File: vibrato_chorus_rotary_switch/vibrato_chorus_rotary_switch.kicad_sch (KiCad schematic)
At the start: 2 parts, among them J1 7-215079-8, SW1 SW_Rotary1x6

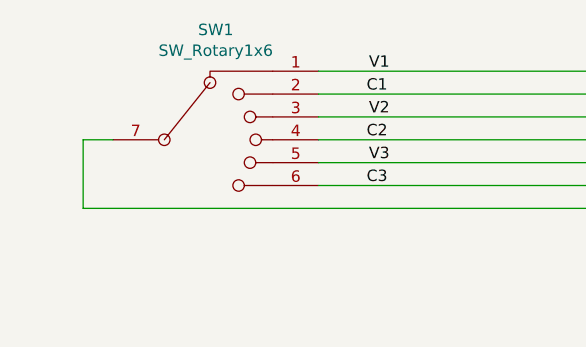
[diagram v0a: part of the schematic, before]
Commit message: A very small PCB to handle the V/C rotary switch selector
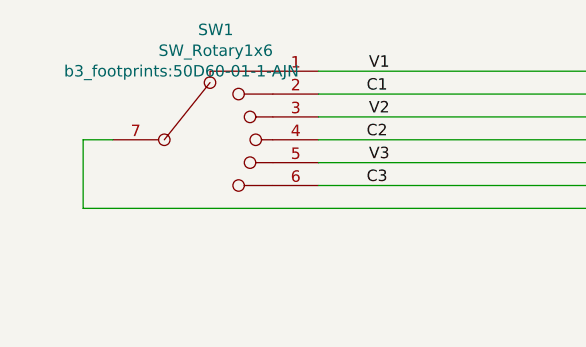
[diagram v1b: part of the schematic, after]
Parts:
- J1: footprint b3_footprints:MicroMatch_2x04_P1.27mm_Vertical -> Connector_TE-Connectivity:TE_Micro-MaTch_215079-8_2x04_P1.27mm_Vertical

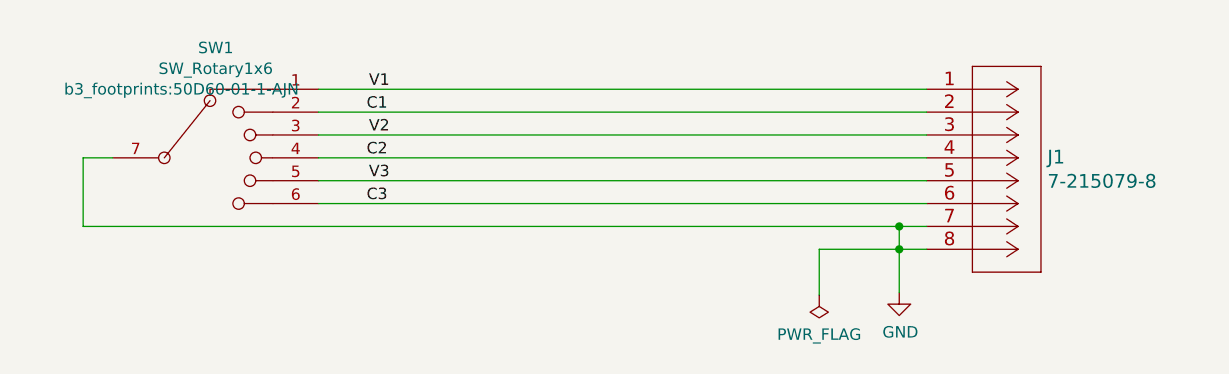
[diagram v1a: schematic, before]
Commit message: The V/C rotary switch is now connected to the new mother board.
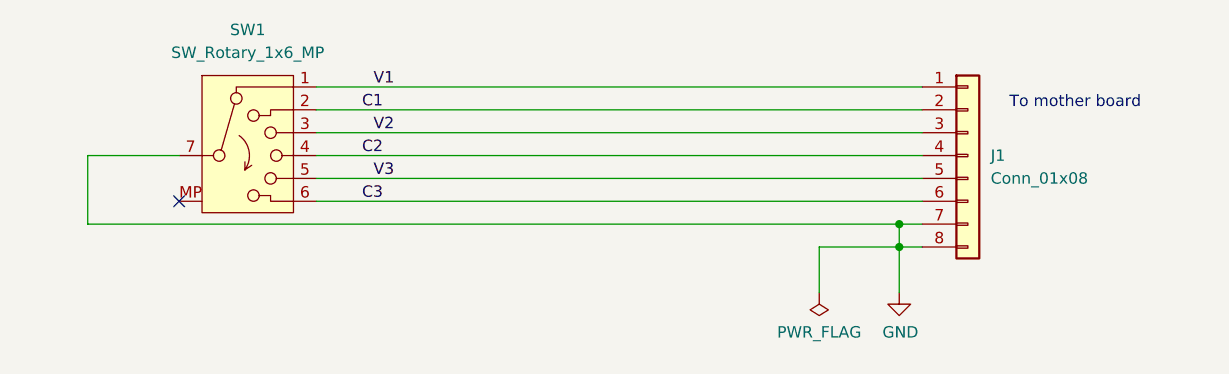
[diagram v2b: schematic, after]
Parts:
- removed J1: 7-215079-8, Connector_TE-Connectivity:TE_Micro-MaTch_215079-8_2x04_P1.27mm_Vertical, symbol b3_connectors_library:7-215079-8
- removed SW1: SW_Rotary1x6, b3_footprints:50D60-01-1-AJN, symbol schematic_library:SW_Rotary1x6
- added J1: Conn_01x08, symbol Connector_Generic:Conn_01x08
- added SW1: SW_Rotary_1x6_MP, symbol Switch:SW_Rotary_1x6_MP
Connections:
- net C1: now also J1.2 (Pin_2), SW1.2
- net C2: now also J1.4 (Pin_4), SW1.4
- net C3: now also J1.6 (Pin_6), SW1.6
- net GND: now also J1.7 (Pin_7), J1.8 (Pin_8), SW1.7
- net V1: now also J1.1 (Pin_1), SW1.1
- net V2: now also J1.3 (Pin_3), SW1.3
- net V3: now also J1.5 (Pin_5), SW1.5
- no-connect marks 0 -> 1
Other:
- note added: "To mother board"

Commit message: New organ architecture with mother board
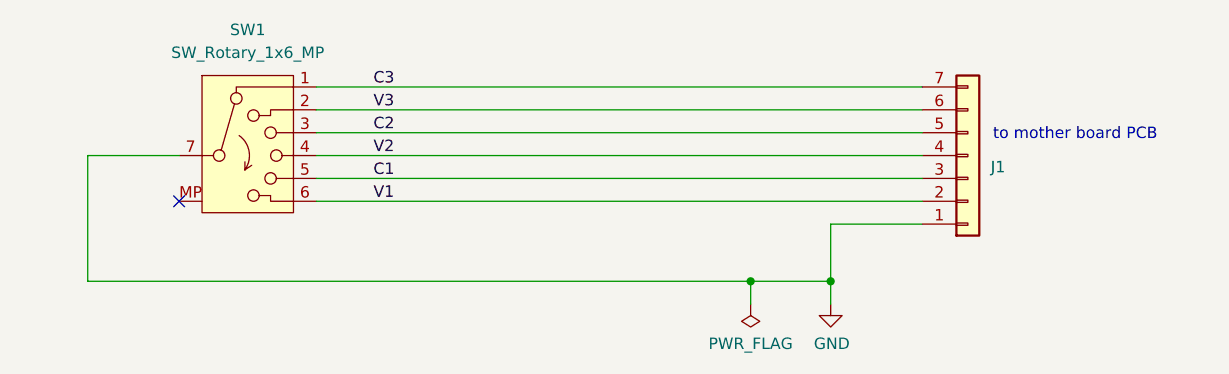
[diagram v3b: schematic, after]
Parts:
- removed J1: Conn_01x08, symbol Connector_Generic:Conn_01x08
- added J1: Conn_01x07, symbol Connector_Generic:Conn_01x07
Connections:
- net C1: now also SW1.5, J1.3 (Pin_3); no longer SW1.2
- net C2: now also SW1.3, J1.5 (Pin_5); no longer SW1.4
- net C3: now also SW1.1, J1.7 (Pin_7); no longer SW1.6
- net GND: now also J1.1 (Pin_1)
- net V1: now also SW1.6, J1.2 (Pin_2); no longer SW1.1
- net V2: now also SW1.4, J1.4 (Pin_4); no longer SW1.3
- net V3: now also SW1.2, J1.6 (Pin_6); no longer SW1.5
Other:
- note added: "to mother board PCB"
- note removed: "To mother board"
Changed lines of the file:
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@@
 (kicad_sch
-	(version 20231120)
+	(version 20250114)
 	(generator "eeschema")
-	(generator_version "8.0")
+	(generator_version "9.0")
 	(paper "A4")
 	(title_block
@@
 		(date "2024-11-12")
 	)
+	(text "to mother board PCB"
+		(exclude_from_sim no)
+		(at 203.454 90.424 0)
+		(effects
+			(font
+				(size 1.27 1.27)
+			)
+			(justify left)
+		)
+	)
 	(junction
-		(at 193.04 100.33)
+		(at 185.42 106.68)
 		(diameter 0)
 		(color 0 0 0 0)
 	)
 	(junction
-		(at 193.04 102.87)
+		(at 176.53 106.68)
 		(diameter 0)
 		(color 0 0 0 0)
@@
 	(wire
 		(pts
-			(xy 102.87 100.33) (xy 193.04 100.33)
-		)
-		(stroke
-			(width 0)
-			(type default)
-		)
-	)
-	(wire
-		(pts
-			(xy 102.87 92.71) (xy 102.87 100.33)
+			(xy 102.87 106.68) (xy 176.53 106.68)
+		)
+		(stroke
+			(width 0)
+			(type default)
+		)
+	)
+	(wire
+		(pts
+			(xy 102.87 92.71) (xy 102.87 106.68)
+		)
+		(stroke
+			(width 0)
+			(type default)
+		)
+	)
+	(wire
+		(pts
+			(xy 185.42 100.33) (xy 195.58 100.33)
 		)
 		(stroke
@@
 	(wire
 		(pts
+			(xy 185.42 106.68) (xy 185.42 109.22)
+		)
+		(stroke
+			(width 0)
+			(type default)
+		)
+	)
+	(wire
+		(pts
 			(xy 128.27 87.63) (xy 195.58 87.63)
 		)
@@
 	(wire
 		(pts
-			(xy 193.04 100.33) (xy 195.58 100.33)
-		)
-		(stroke
-			(width 0)
-			(type default)
-		)
-	)
-	(wire
-		(pts
-			(xy 193.04 102.87) (xy 193.04 107.95)
+			(xy 128.27 95.25) (xy 195.58 95.25)
+		)
+		(stroke
+			(width 0)
+			(type default)
+		)
+	)
+	(wire
+		(pts
+			(xy 185.42 100.33) (xy 185.42 106.68)
 		)
 		(stroke
@@
 	(wire
 		(pts
-			(xy 184.15 107.95) (xy 184.15 102.87)
-		)
-		(stroke
-			(width 0)
-			(type default)
-		)
-	)
-	(wire
-		(pts
-			(xy 184.15 102.87) (xy 193.04 102.87)
-		)
-		(stroke
-			(width 0)
-			(type default)
-		)
-	)
-	(wire
-		(pts
-			(xy 195.58 95.25) (xy 128.27 95.25)
-		)
-		(stroke
-			(width 0)
-			(type default)
-		)
-	)
-	(wire
-		(pts
-			(xy 195.58 102.87) (xy 193.04 102.87)
-		)
-		(stroke
-			(width 0)
-			(type default)
-		)
-	)
-	(wire
-		(pts
-			(xy 195.58 90.17) (xy 128.27 90.17)
-		)
-		(stroke
-			(width 0)
-			(type default)
-		)
-	)
-	(wire
-		(pts
-			(xy 193.04 102.87) (xy 193.04 100.33)
-		)
-		(stroke
-			(width 0)
-			(type default)
-		)
-	)
-	(text "To mother board"
-		(exclude_from_sim no)
-		(at 212.598 86.868 0)
-		(effects
-			(font
-				(size 1.27 1.27)
-			)
+			(xy 176.53 106.68) (xy 185.42 106.68)
+		)
+		(stroke
+			(width 0)
+			(type default)
+		)
+	)
+	(wire
+		(pts
+			(xy 128.27 90.17) (xy 195.58 90.17)
+		)
+		(stroke
+			(width 0)
+			(type default)
+		)
+	)
+	(wire
+		(pts
+			(xy 176.53 109.22) (xy 176.53 106.68)
+		)
+		(stroke
+			(width 0)
+			(type default)
 		)
 	)
 	(label "C1"
-		(at 133.35 87.63 0)
-		(fields_autoplaced yes)
+		(at 134.62 95.25 0)
 		(effects
 			(font
@@
 	)
 	(label "C3"
-		(at 133.35 97.79 0)
-		(fields_autoplaced yes)
+		(at 134.62 85.09 0)
 		(effects
 			(font
@@
 	)
 	(label "V1"
-		(at 134.62 85.09 0)
-		(fields_autoplaced yes)
+		(at 134.62 97.79 0)
 		(effects
 			(font
@@
 	)
 	(label "V3"
-		(at 134.62 95.25 0)
-		(fields_autoplaced yes)
+		(at 134.62 87.63 0)
 		(effects
 			(font
@@
 	)
 	(label "V2"
+		(at 134.62 92.71 0)
+		(effects
+			(font
+				(size 1.27 1.27)
+			)
+			(justify left bottom)
+		)
+	)
+	(label "C2"
 		(at 134.62 90.17 0)
-		(fields_autoplaced yes)
-		(effects
-			(font
-				(size 1.27 1.27)
-			)
-			(justify left bottom)
-		)
-	)
-	(label "C2"
-		(at 133.35 92.71 0)
-		(fields_autoplaced yes)
 		(effects
 			(font
@@
 	(symbol
 		(lib_id "power:GND")
-		(at 193.04 107.95 0)
+		(at 185.42 109.22 0)
 		(unit 1)
 		(exclude_from_sim no)
@@
 		(dnp no)
 		(property "Reference" "#PWR01"
-			(at 193.04 114.3 0)
+			(at 185.42 115.57 0)
 			(effects
 				(font
@@
 		)
 		(property "Value" "GND"
-			(at 193.167 112.3442 0)
+			(at 185.547 113.6142 0)
 			(effects
 				(font
@@
 		)
 		(property "Footprint" ""
-			(at 193.04 107.95 0)
+			(at 185.42 109.22 0)
 			(effects
 				(font
@@
 		)
 		(property "Datasheet" ""
-			(at 193.04 107.95 0)
+			(at 185.42 109.22 0)
 			(effects
 				(font
@@
 		)
 		(property "Description" "Power symbol creates a global label with name \"GND\" , ground"
-			(at 193.04 107.95 0)
+			(at 185.42 109.22 0)
 			(effects
 				(font
@@
 	(symbol
 		(lib_id "power:PWR_FLAG")
-		(at 184.15 107.95 0)
+		(at 176.53 109.22 0)
 		(mirror x)
 		(unit 1)
@@
 		(dnp no)
 		(property "Reference" "#FLG01"
-			(at 184.15 109.855 0)
+			(at 176.53 111.125 0)
 			(effects
 				(font
@@
 		)
 		(property "Value" "PWR_FLAG"
-			(at 184.15 112.3442 0)
+			(at 176.53 113.6142 0)
 			(effects
 				(font
@@
 		)
 		(property "Footprint" ""
-			(at 184.15 107.95 0)
+			(at 176.53 109.22 0)
 			(effects
 				(font
@@
 		)
 		(property "Datasheet" "~"
-			(at 184.15 107.95 0)
+			(at 176.53 109.22 0)
 			(effects
 				(font
@@
 		)
 		(property "Description" "Special symbol for telling ERC where power comes from"
-			(at 184.15 107.95 0)
+			(at 176.53 109.22 0)
 			(effects
 				(font
@@
 	)
 	(symbol
-		(lib_id "Connector_Generic:Conn_01x08")
+		(lib_id "Connector_Generic:Conn_01x07")
 		(at 200.66 92.71 0)
+		(mirror x)
 		(unit 1)
 		(exclude_from_sim no)
@@
 		(on_board yes)
 		(dnp no)
-		(fields_autoplaced yes)
 		(property "Reference" "J1"
-			(at 203.2 92.7099 0)
+			(at 203.2 93.9801 0)
 			(effects
 				(font
@@
 			)
 		)
-		(property "Value" "Conn_01x08"
-			(at 203.2 95.2499 0)
+		(property "Value" "Conn_01x07"
+			(at 203.2 91.4401 0)
 			(effects
 				(font
@@
 				)
 				(justify left)
+				(hide yes)
 			)
 		)
@@
 			)
 		)
-		(property "Description" "Generic connector, single row, 01x08, script generated (kicad-library-utils/schlib/autogen/connector/)"
+		(property "Description" "Generic connector, single row, 01x07, script generated (kicad-library-utils/schlib/autogen/connector/)"
 			(at 200.66 92.71 0)
 			(effects
@@
 			)
 		)
+		(pin "2"
+		)
+		(pin "1"
+		)
 		(pin "7"
 		)
-		(pin "8"
+		(pin "4"
 		)
 		(pin "3"
@@
 		(pin "6"
 		)
-		(pin "2"
-		)
-		(pin "4"
-		)
 		(pin "5"
-		)
-		(pin "1"
 		)
 		(instances
@@
 		)
 	)
+	(embedded_fonts no)
 )
